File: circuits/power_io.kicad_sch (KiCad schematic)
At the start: 55 parts, among them J5 24V DC IN, J6 CONN_RJ45, U11 AP2112K-3.3, U12 INA4180A1, U13 LM4040C50 5V, U14 AD7606BSTZ-4, U15 AP63205WU-7 5V BUCK, U16 AP63200WU-7 10.7V BUCK

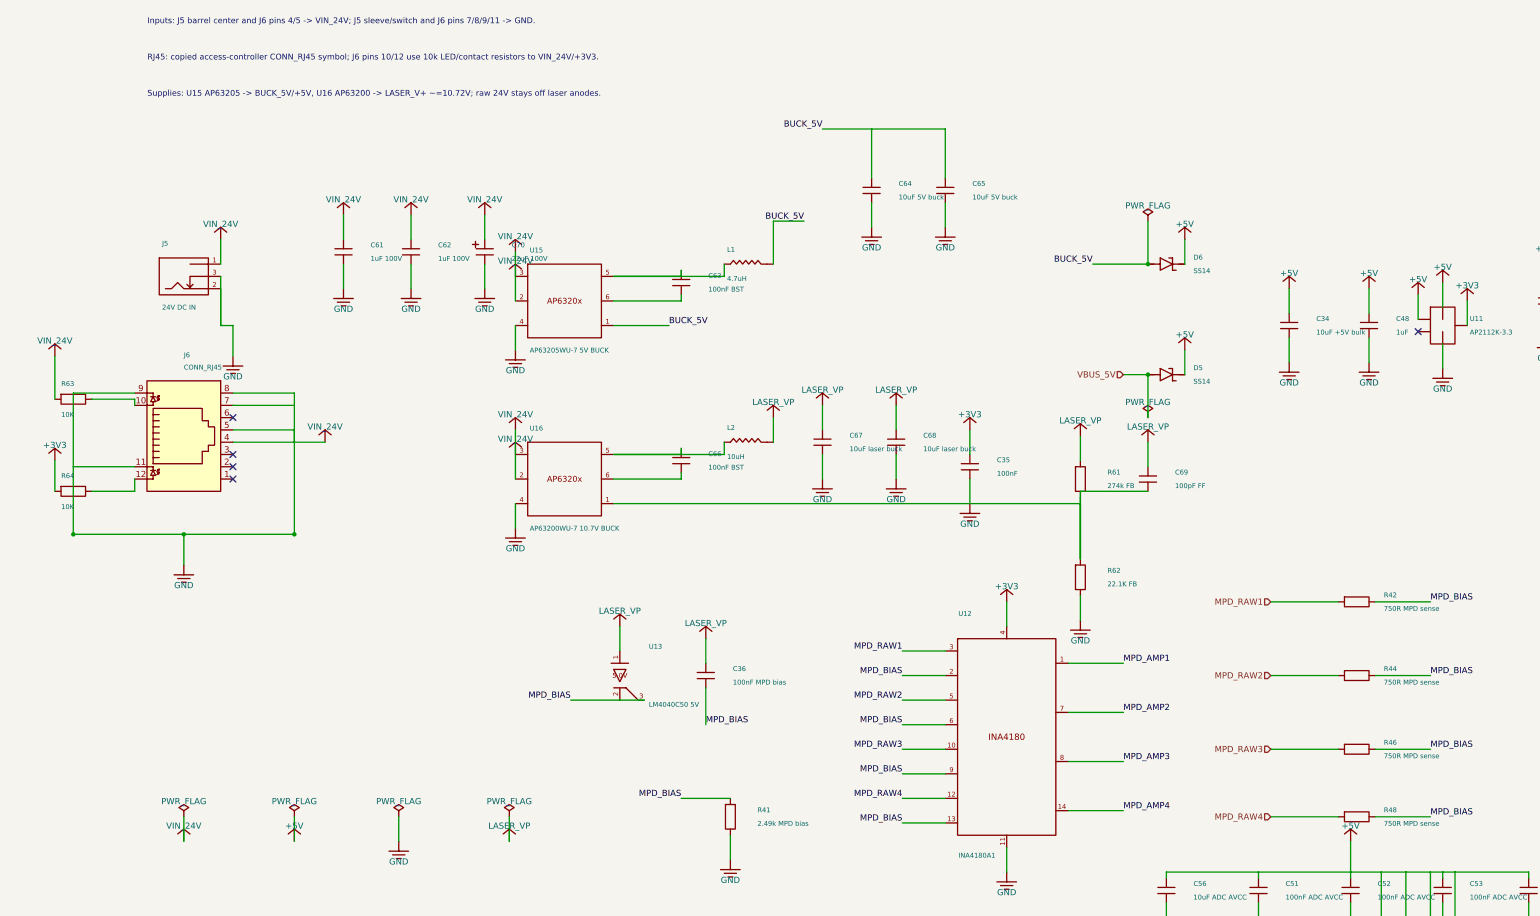
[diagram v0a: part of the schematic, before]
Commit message: Datasheet system audit: new verification checks, part notes, and PCB revisions
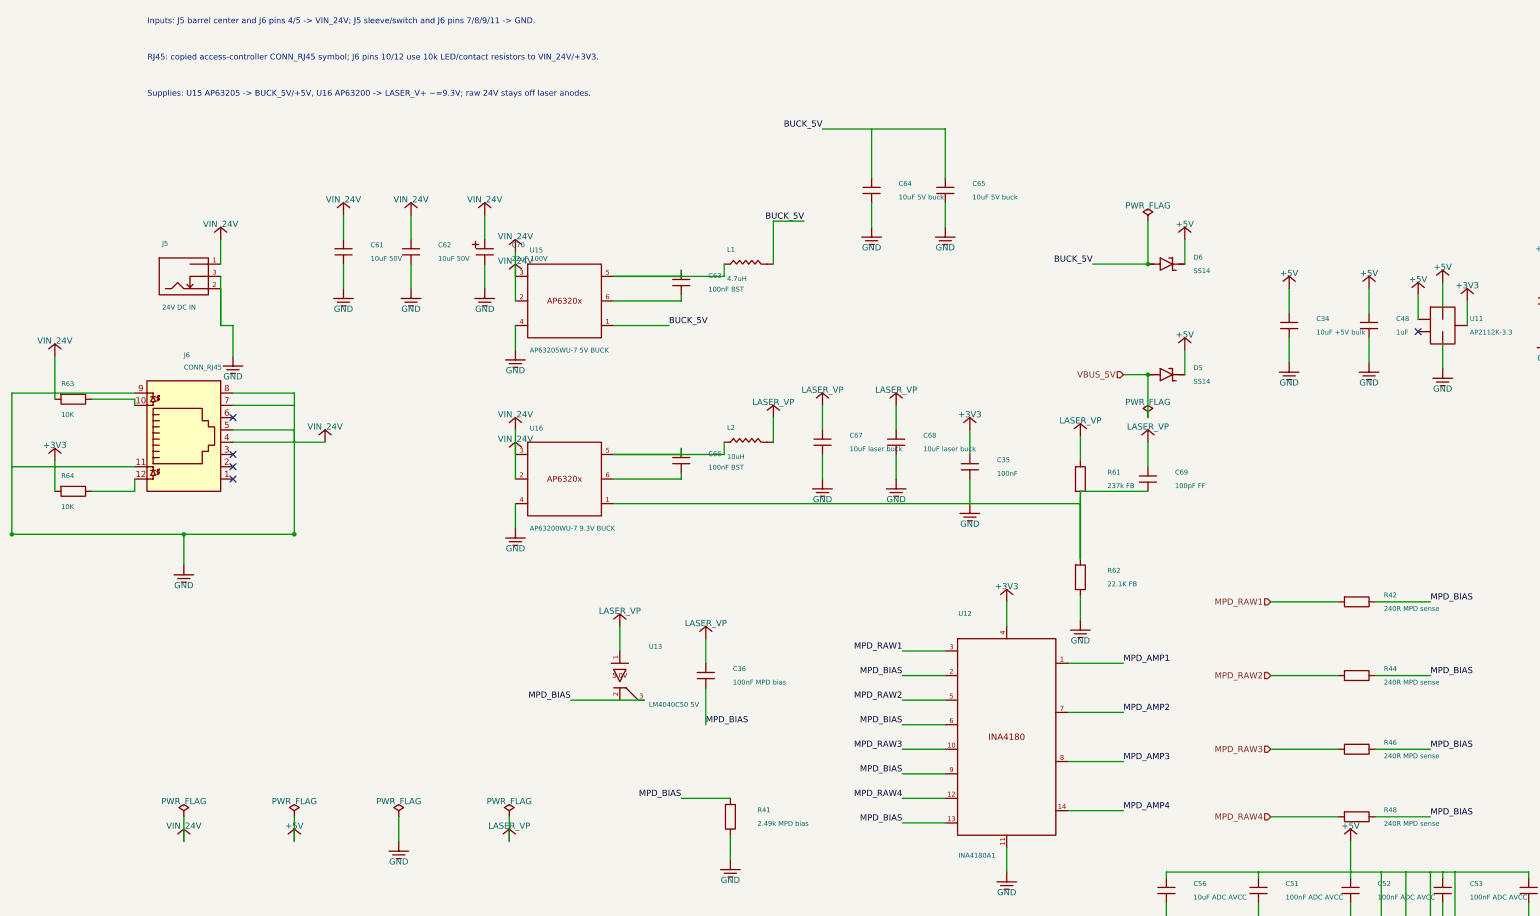
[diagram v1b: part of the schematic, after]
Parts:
- C61, C62: value 1uF 100V -> 10uF 50V; LCSC C13832 -> C3080136; Part Number CL31B105KCHNNNE -> CL31B106KBHNNNE
- R42, R44, R46, R48: value 750R MPD sense -> 240R MPD sense; LCSC C114635 -> C114613; Part Number RC0603FR-07750RL -> RC0603FR-07240RL
- R61: value 274k FB -> 237k FB; LCSC C2942027 -> C2942028; Part Number FRC0603F2743TS -> FRC0603F2373TS
- U16: value AP63200WU-7 10.7V BUCK -> AP63200WU-7 9.3V BUCK
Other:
- note added: "Supplies: U15 AP63205 -> BUCK_5V/+5V, U16 AP63200 -> LASER_V+ ~=9.3V; raw 24V stays off laser anodes."
- note removed: "Supplies: U15 AP63205 -> BUCK_5V/+5V, U16 AP63200 -> LASER_V+ ~=10.72V; raw 24V stays off laser anodes."

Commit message: Checkpoint laser controller layout cleanup
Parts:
- C61, C62: LCSC C3080136 -> C89632
- R61: LCSC C2942028 -> C2998117
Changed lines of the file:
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@@
     (property "Datasheet" "" (at 115.57 85.09 0) (effects (font (size 1.0 1.0)) hide))
     (property "Part Number" "CL31B106KBHNNNE" (at 115.57 85.09 0) (effects (font (size 1.0 1.0)) hide))
-    (property "LCSC" "C3080136" (at 115.57 85.09 0) (effects (font (size 1.0 1.0)) hide))
+    (property "LCSC" "C89632" (at 115.57 85.09 0) (effects (font (size 1.0 1.0)) hide))
     (pin "1")
     (pin "2")
@@
     (property "Datasheet" "" (at 129.54 85.09 0) (effects (font (size 1.0 1.0)) hide))
     (property "Part Number" "CL31B106KBHNNNE" (at 129.54 85.09 0) (effects (font (size 1.0 1.0)) hide))
-    (property "LCSC" "C3080136" (at 129.54 85.09 0) (effects (font (size 1.0 1.0)) hide))
+    (property "LCSC" "C89632" (at 129.54 85.09 0) (effects (font (size 1.0 1.0)) hide))
     (pin "1")
     (pin "2")
@@
     (property "Datasheet" "" (at 267.97 132.08 0) (effects (font (size 1.0 1.0)) hide))
     (property "Part Number" "FRC0603F2373TS" (at 267.97 132.08 0) (effects (font (size 1.0 1.0)) hide))
-    (property "LCSC" "C2942028" (at 267.97 132.08 0) (effects (font (size 1.0 1.0)) hide))
-    (pin "1")
-    (pin "2")
+    (property "LCSC" "C2998117" (at 267.97 132.08 0) (effects (font (size 1.0 1.0)) hide))
+    (pin "1")
+    (pin "2")

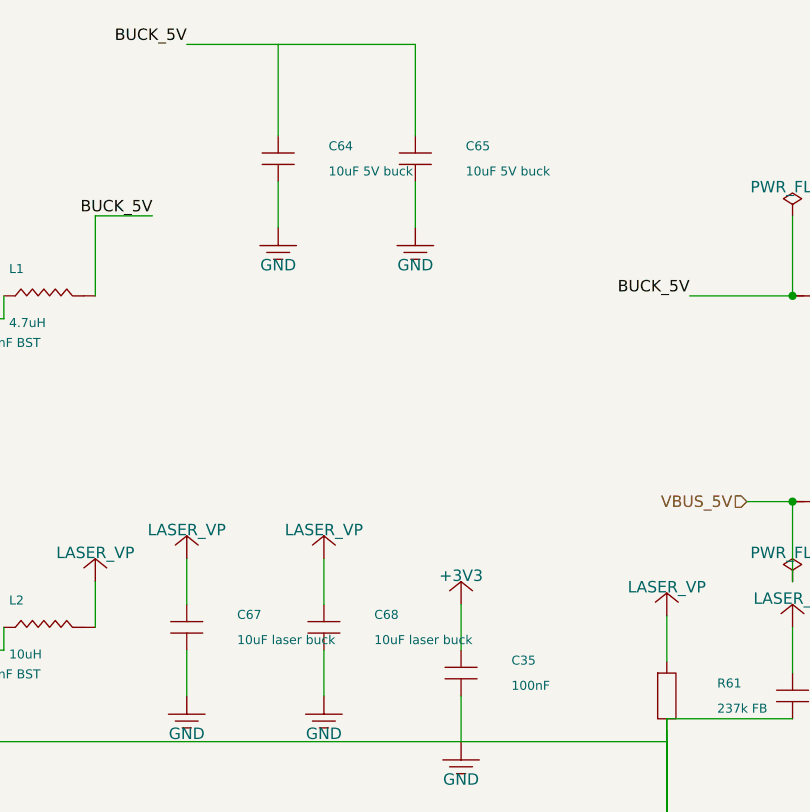
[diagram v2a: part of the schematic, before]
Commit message: Increase AP632 buck output capacitance
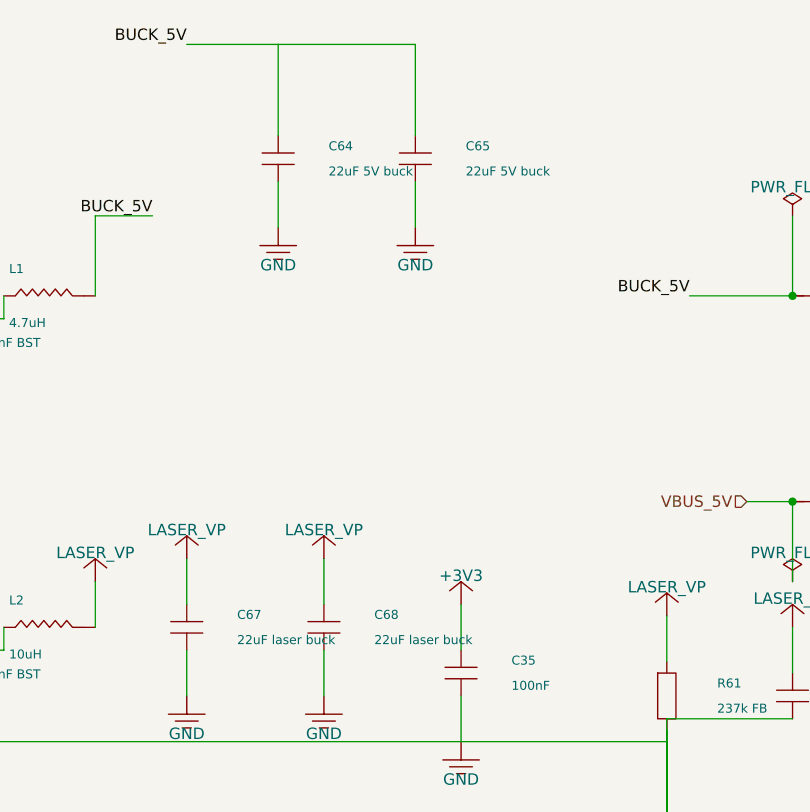
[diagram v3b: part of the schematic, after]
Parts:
- C64, C65: value 10uF 5V buck -> 22uF 5V buck; LCSC C318691 -> C45783; Part Number CL21A106KAYNNNG -> CL21A226MAQNNNE
- C67, C68: value 10uF laser buck -> 22uF laser buck; LCSC C318691 -> C45783; Part Number CL21A106KAYNNNG -> CL21A226MAQNNNE
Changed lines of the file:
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@@
     (in_bom yes) (on_board yes) (dnp no)
     (property "Reference" "C64" (at 230.39 70.99 0) (effects (font (size 1.0 1.0)) (justify left)))
-    (property "Value" "10uF 5V buck" (at 230.39 73.79 0) (effects (font (size 1.0 1.0)) (justify left)))
+    (property "Value" "22uF 5V buck" (at 230.39 73.79 0) (effects (font (size 1.0 1.0)) (justify left)))
     (property "Footprint" "Capacitor_SMD:C_0805_2012Metric_Pad1.18x1.45mm_HandSolder" (at 224.79 72.39 0) (effects (font (size 1.0 1.0)) hide))
     (property "Datasheet" "" (at 224.79 72.39 0) (effects (font (size 1.0 1.0)) hide))
-    (property "Part Number" "CL21A106KAYNNNG" (at 224.79 72.39 0) (effects (font (size 1.0 1.0)) hide))
-    (property "LCSC" "C318691" (at 224.79 72.39 0) (effects (font (size 1.0 1.0)) hide))
+    (property "Part Number" "CL21A226MAQNNNE" (at 224.79 72.39 0) (effects (font (size 1.0 1.0)) hide))
+    (property "LCSC" "C45783" (at 224.79 72.39 0) (effects (font (size 1.0 1.0)) hide))
     (pin "1")
     (pin "2")
@@
     (in_bom yes) (on_board yes) (dnp no)
     (property "Reference" "C65" (at 245.63 70.99 0) (effects (font (size 1.0 1.0)) (justify left)))
-    (property "Value" "10uF 5V buck" (at 245.63 73.79 0) (effects (font (size 1.0 1.0)) (justify left)))
+    (property "Value" "22uF 5V buck" (at 245.63 73.79 0) (effects (font (size 1.0 1.0)) (justify left)))
     (property "Footprint" "Capacitor_SMD:C_0805_2012Metric_Pad1.18x1.45mm_HandSolder" (at 240.03 72.39 0) (effects (font (size 1.0 1.0)) hide))
     (property "Datasheet" "" (at 240.03 72.39 0) (effects (font (size 1.0 1.0)) hide))
-    (property "Part Number" "CL21A106KAYNNNG" (at 240.03 72.39 0) (effects (font (size 1.0 1.0)) hide))
-    (property "LCSC" "C318691" (at 240.03 72.39 0) (effects (font (size 1.0 1.0)) hide))
+    (property "Part Number" "CL21A226MAQNNNE" (at 240.03 72.39 0) (effects (font (size 1.0 1.0)) hide))
+    (property "LCSC" "C45783" (at 240.03 72.39 0) (effects (font (size 1.0 1.0)) hide))
     (pin "1")
     (pin "2")
@@
     (in_bom yes) (on_board yes) (dnp no)
     (property "Reference" "C67" (at 220.23 123.06 0) (effects (font (size 1.0 1.0)) (justify left)))
-    (property "Value" "10uF laser buck" (at 220.23 125.86 0) (effects (font (size 1.0 1.0)) (justify left)))
+    (property "Value" "22uF laser buck" (at 220.23 125.86 0) (effects (font (size 1.0 1.0)) (justify left)))
     (property "Footprint" "Capacitor_SMD:C_0805_2012Metric_Pad1.18x1.45mm_HandSolder" (at 214.63 124.46 0) (effects (font (size 1.0 1.0)) hide))
     (property "Datasheet" "" (at 214.63 124.46 0) (effects (font (size 1.0 1.0)) hide))
-    (property "Part Number" "CL21A106KAYNNNG" (at 214.63 124.46 0) (effects (font (size 1.0 1.0)) hide))
-    (property "LCSC" "C318691" (at 214.63 124.46 0) (effects (font (size 1.0 1.0)) hide))
+    (property "Part Number" "CL21A226MAQNNNE" (at 214.63 124.46 0) (effects (font (size 1.0 1.0)) hide))
+    (property "LCSC" "C45783" (at 214.63 124.46 0) (effects (font (size 1.0 1.0)) hide))
     (pin "1")
     (pin "2")
@@
     (in_bom yes) (on_board yes) (dnp no)
     (property "Reference" "C68" (at 235.47 123.06 0) (effects (font (size 1.0 1.0)) (justify left)))
-    (property "Value" "10uF laser buck" (at 235.47 125.86 0) (effects (font (size 1.0 1.0)) (justify left)))
+    (property "Value" "22uF laser buck" (at 235.47 125.86 0) (effects (font (size 1.0 1.0)) (justify left)))
     (property "Footprint" "Capacitor_SMD:C_0805_2012Metric_Pad1.18x1.45mm_HandSolder" (at 229.87 124.46 0) (effects (font (size 1.0 1.0)) hide))
     (property "Datasheet" "" (at 229.87 124.46 0) (effects (font (size 1.0 1.0)) hide))
-    (property "Part Number" "CL21A106KAYNNNG" (at 229.87 124.46 0) (effects (font (size 1.0 1.0)) hide))
-    (property "LCSC" "C318691" (at 229.87 124.46 0) (effects (font (size 1.0 1.0)) hide))
-    (pin "1")
-    (pin "2")
+    (property "Part Number" "CL21A226MAQNNNE" (at 229.87 124.46 0) (effects (font (size 1.0 1.0)) hide))
+    (property "LCSC" "C45783" (at 229.87 124.46 0) (effects (font (size 1.0 1.0)) hide))
+    (pin "1")
+    (pin "2")

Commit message: Checkpoint laser controller fab parity package
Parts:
- removed J5: 24V DC IN, Open_Automation:BarrelJack_OD5.5_ID2.5, symbol viv:BARREL_JACK_SWITCH
- added U15: AP63205WU-7 5V BUCK, Package_TO_SOT_SMD:TSOT-23-6, symbol viv:AP6320X_TSOT6
- J5: renamed from U15; value AP63205WU-7 5V BUCK -> 24V DC IN; footprint Package_TO_SOT_SMD:TSOT-23-6 -> Open_Automation:BarrelJack_OD5.5_ID2.5; symbol viv:AP6320X_TSOT6 -> viv:BARREL_JACK_SWITCH; LCSC C2071056 -> C194407; Part Number AP63205WU-7 -> DC-470-2.1GP
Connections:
- net BUCK_5V: now also U15.1 (FB); no longer J5.1 (FB)
- net GND: now also J5.1, U15.2 (EN), U15.3 (IN), U15.4 (GND); no longer J5.4 (GND)
- net RJ45_PWR_DETECT: now reaches J6.10, R63.2
- net RJ45_LED_CONTACT: now reaches J6.12, R64.2
- net BUCK5_SW: now reaches C63.1, L1.1
- net BUCK5_SW: now also U15.5 (SW); no longer J5.5 (SW)
- net BUCK5_BST: now reaches C63.2
- net BUCK5_BST: now also U15.6 (BST); no longer J5.6 (BST)
- net LASER_BUCK_FB: now reaches C69.2, R61.2, R62.1, U16.1 (FB)
- net LASER_BUCK_SW: now reaches C66.1, L2.1, U16.5 (SW)
- net LASER_BUCK_BST: now reaches C66.2, U16.6 (BST)
- net ADC_CREG1: now reaches C57.1, U14.36 (REGCAP)
- net ADC_CREG2: now reaches C58.1, U14.39 (REGCAP)
- net ADC_CREFIN: now reaches C59.1, U14.42 (REFIN/REFOUT)
- net ADC_REFCAP: now reaches C60.1, U14.44 (REFCAPA), U14.45 (REFCAPB)
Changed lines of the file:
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@@
   (no_connect (at 337.82 101.6))
   (no_connect (at 368.3 274.32))
+  (label "RJ45_PWR_DETECT" (at 63.5 115.57 0) (effects (font (size 1.27 1.27)) (justify right bottom)))
+  (label "RJ45_LED_CONTACT" (at 63.5 134.62 0) (effects (font (size 1.27 1.27)) (justify right bottom)))
+  (label "BUCK5_SW" (at 171.45 90.17 0) (effects (font (size 1.27 1.27)) (justify left bottom)))
+  (label "BUCK5_BST" (at 171.45 95.25 0) (effects (font (size 1.27 1.27)) (justify left bottom)))
   (label "BUCK_5V" (at 210.82 78.74 0) (effects (font (size 1.27 1.27)) (justify right bottom)))
   (label "BUCK_5V" (at 182.88 100.33 0) (effects (font (size 1.27 1.27)) (justify left bottom)))
@@
   (label "BUCK_5V" (at 214.63 59.69 0) (effects (font (size 1.27 1.27)) (justify right bottom)))
   (hierarchical_label "VBUS_5V" (shape input) (at 276.86 110.49 0) (effects (font (size 1.27 1.27)) (justify right)))
+  (label "LASER_BUCK_SW" (at 171.45 127 0) (effects (font (size 1.27 1.27)) (justify left bottom)))
+  (label "LASER_BUCK_BST" (at 171.45 132.08 0) (effects (font (size 1.27 1.27)) (justify left bottom)))
+  (label "LASER_BUCK_FB" (at 267.97 148.59 0) (effects (font (size 1.27 1.27)) (justify left bottom)))
   (hierarchical_label "VOUT1" (shape input) (at 307.34 261.62 0) (effects (font (size 1.27 1.27)) (justify right)))
   (hierarchical_label "VOUT2" (shape input) (at 307.34 266.7 0) (effects (font (size 1.27 1.27)) (justify right)))
@@
   (hierarchical_label "ADC_MISO_A" (shape output) (at 378.46 276.86 0) (effects (font (size 1.27 1.27)) (justify left)))
   (hierarchical_label "ADC_MISO_B" (shape output) (at 378.46 279.4 0) (effects (font (size 1.27 1.27)) (justify left)))
+  (label "ADC_CREG1" (at 285.75 285.75 0) (effects (font (size 1.27 1.27)) (justify left bottom)))
+  (label "ADC_CREG2" (at 274.32 292.1 0) (effects (font (size 1.27 1.27)) (justify left bottom)))
+  (label "ADC_CREFIN" (at 261.62 298.45 0) (effects (font (size 1.27 1.27)) (justify left bottom)))
+  (label "ADC_REFCAP" (at 248.92 304.8 0) (effects (font (size 1.27 1.27)) (justify left bottom)))
   (label "MPD_BIAS" (at 162.56 177.8 0) (effects (font (size 1.27 1.27)) (justify right bottom)))
   (label "MPD_BIAS" (at 190.5 182.88 0) (effects (font (size 1.27 1.27)) (justify left bottom)))
